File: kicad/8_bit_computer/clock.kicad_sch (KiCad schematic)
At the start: 0 parts

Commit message: Astable clock
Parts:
- added C4: 220uF, Capacitor_THT:CP_Radial_D10.0mm_P5.00mm, symbol Device:C_Polarized_US
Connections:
- new net +5V: C4.1
- new net GND: C4.2
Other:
- added sheet Astable Timer (astable_timer.kicad_sch)
- title: (none) -> Clock Module

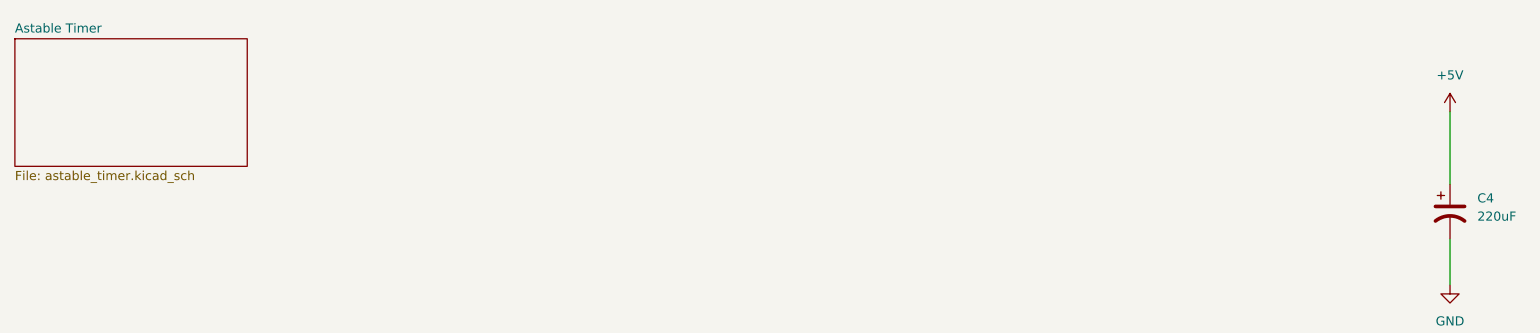
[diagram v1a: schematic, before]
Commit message: Bistable and Monstable Clocks
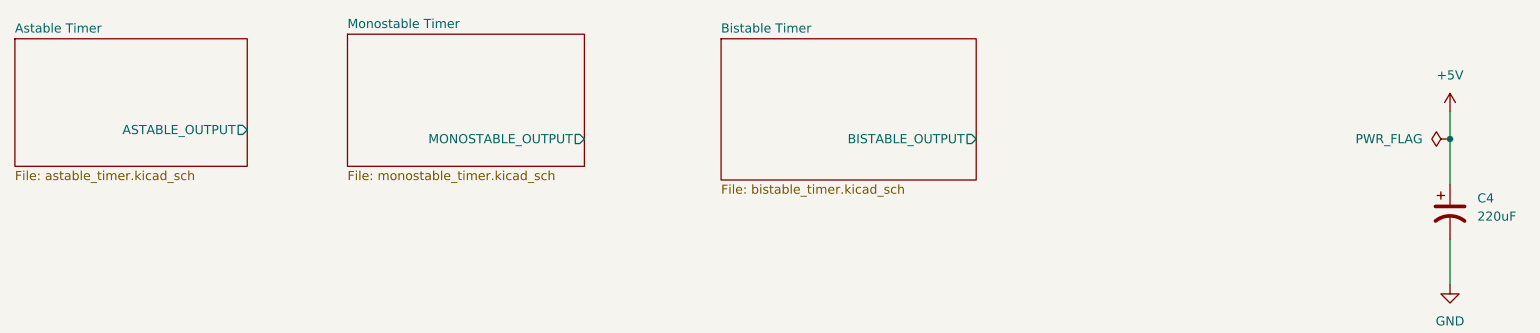
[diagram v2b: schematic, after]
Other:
- added sheet Bistable Timer (bistable_timer.kicad_sch)
- added sheet Monostable Timer (monostable_timer.kicad_sch)
- sheet Astable Timer ports: added ASTABLE_OUTPUT; removed none
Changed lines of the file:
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@@
 		(rev "0")
+	)
+	(junction
+		(at 245.11 44.45)
+		(diameter 0)
+		(color 0 0 0 0)
 	)
 	(wire
 		(pts
-			(xy 245.11 40.64) (xy 245.11 50.8)
+			(xy 245.11 40.64) (xy 245.11 44.45)
 		)
 		(stroke
@@
 		(pts
 			(xy 245.11 58.42) (xy 245.11 64.77)
+		)
+		(stroke
+			(width 0)
+			(type default)
+		)
+	)
+	(wire
+		(pts
+			(xy 245.11 44.45) (xy 245.11 50.8)
 		)
 		(stroke
@@
 	)
 	(symbol
+		(lib_id "power:PWR_FLAG")
+		(at 245.11 44.45 90)
+		(unit 1)
+		(exclude_from_sim no)
+		(in_bom yes)
+		(on_board yes)
+		(dnp no)
+		(fields_autoplaced yes)
+		(property "Reference" "#FLG03"
+			(at 243.205 44.45 0)
+			(effects
+				(font
+					(size 1.27 1.27)
+				)
+				(hide yes)
+			)
+		)
+		(property "Value" "PWR_FLAG"
+			(at 241.3 44.4499 90)
+			(effects
+				(font
+					(size 1.27 1.27)
+				)
+				(justify left)
+			)
+		)
+		(property "Footprint" ""
+			(at 245.11 44.45 0)
+			(effects
+				(font
+					(size 1.27 1.27)
+				)
+				(hide yes)
+			)
+		)
+		(property "Datasheet" "~"
+			(at 245.11 44.45 0)
+			(effects
+				(font
+					(size 1.27 1.27)
+				)
+				(hide yes)
+			)
+		)
+		(property "Description" "Special symbol for telling ERC where power comes from"
+			(at 245.11 44.45 0)
+			(effects
+				(font
+					(size 1.27 1.27)
+				)
+				(hide yes)
+			)
+		)
+		(pin "1"
+		)
+		(instances
+			(project ""
+				(path "/24dbb59b-fc31-4588-b2ee-d18f20639e07/62eb35ce-6b42-428c-8bc5-4f1b242b0bef"
+					(reference "#FLG03")
+					(unit 1)
+				)
+			)
+		)
+	)
+	(symbol
 		(lib_id "Device:C_Polarized_US")
 		(at 245.11 54.61 0)
@@
 			)
 		)
+		(pin "ASTABLE_OUTPUT" output
+			(at 77.47 43.18 0)
+			(effects
+				(font
+					(size 1.27 1.27)
+				)
+				(justify right)
+			)
+		)
 		(instances
 			(project "8_bit_computer"
@@
 				)
 			)
+		)
+	)
+	(sheet
+		(at 143.51 30.48)
+		(size 35.56 19.685)
+		(fields_autoplaced yes)
+		(stroke
+			(width 0.1524)
+			(type solid)
+		)
+		(fill
+			(color 0 0 0 0.0000)
+		)
+		(property "Sheetname" "Bistable Timer"
+			(at 143.51 29.7684 0)
+			(effects
+				(font
+					(size 1.27 1.27)
+				)
+				(justify left bottom)
+			)
+		)
+		(property "Sheetfile" "bistable_timer.kicad_sch"
+			(at 143.51 50.7496 0)
+			(effects
+				(font
+					(size 1.27 1.27)
+				)
+				(justify left top)
+			)
+		)
+		(pin "BISTABLE_OUTPUT" output
+			(at 179.07 44.45 0)
+			(effects
+				(font
+					(size 1.27 1.27)
+				)
+				(justify right)
+			)
+		)
+		(instances
+			(project "8_bit_computer"
+				(path "/24dbb59b-fc31-4588-b2ee-d18f20639e07/62eb35ce-6b42-428c-8bc5-4f1b242b0bef"
+					(page "5")
+				)
+			)
+		)
+	)
+	(sheet
+		(at 91.44 29.845)
+		(size 33.02 18.415)
+		(fields_autoplaced yes)
+		(stroke
+			(width 0.1524)
+			(type solid)
+		)
+		(fill
+			(color 0 0 0 0.0000)
+		)
+		(property "Sheetname" "Monostable Timer"
+			(at 91.44 29.1334 0)
+			(effects
+				(font
+					(size 1.27 1.27)
+				)
+				(justify left bottom)
+			)
+		)
+		(property "Sheetfile" "monostable_timer.kicad_sch"
+			(at 91.44 48.8446 0)
+			(effects
+				(font
+					(size 1.27 1.27)
+				)
+				(justify left top)
+			)
+		)
+		(pin "MONOSTABLE_OUTPUT" output
+			(at 124.46 44.45 0)
+			(effects
+				(font
+					(size 1.27 1.27)
+				)
+				(justify right)
+			)
+		)
+		(instances
+			(project "8_bit_computer"
+				(path "/24dbb59b-fc31-4588-b2ee-d18f20639e07/62eb35ce-6b42-428c-8bc5-4f1b242b0bef"
+					(page "4")
+				)
+			)

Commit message: Functional 8 bit computer clock
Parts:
- added C10, C12, C13: 0.1 uF, Capacitor_THT:C_Disc_D5.0mm_W2.5mm_P2.50mm, symbol Device:C
- added D4: LED Blue, LED_THT:LED_D5.0mm, symbol Device:LED
- added R5: 220, Resistor_THT:R_Axial_DIN0207_L6.3mm_D2.5mm_P7.62mm_Horizontal, symbol Device:R
- added U4: 74LS32, Package_DIP:DIP-14_W7.62mm, symbol 74xx:74LS32
- added U5: 74LS08, Package_DIP:DIP-14_W7.62mm, symbol 74xx:74LS08
- added U6: 74LS04, Package_DIP:DIP-14_W7.62mm, symbol 74xx:74LS04
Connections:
- net +5V: now also C10.2, C12.2, C13.2, U4.14 (VCC), U5.14 (VCC), U6.14 (VCC)
- net Astable Timer/ASTABLE_OUTPUT: now also U5.1
- net Bistable Timer/BISTABLE_OUTPUT: now also U5.2, U6.1
- net GND: now also C10.1, C12.1, C13.1, R5.2, U4.10, U4.12, U4.13, U4.4, U4.5, U4.7 (GND), U4.9, U5.12, U5.13, U5.7 (GND), U6.11, U6.5, U6.7 (GND), U6.9
- net Monostable Timer/MONOSTABLE_OUTPUT: now also U5.5
- new net: U5.4, U6.2
- new net: U4.2, U5.6
- new net: U5.10, U6.4
- new net: U4.1, U5.3
- new net: D4.1 (K), R5.1
- new net: U4.3, U5.9
- new net CLK: D4.2 (A), U5.8, U6.13
- new net HLT: U6.3
- new net ~{CLK}: U6.12
- no-connect marks 0 -> 7
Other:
- note added: "Unused"
- moved on the sheet: C4

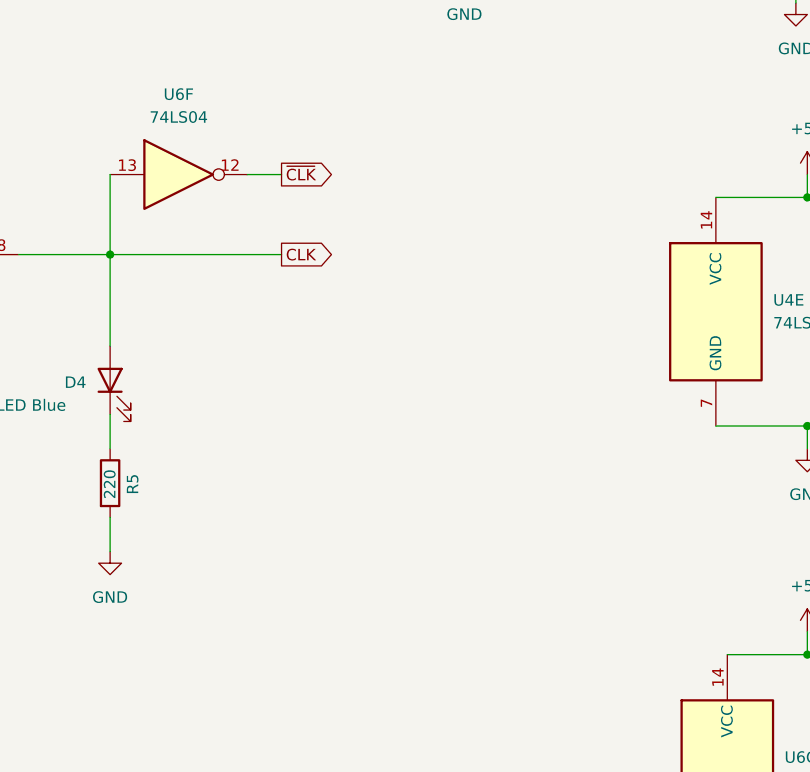
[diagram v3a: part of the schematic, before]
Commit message: clk_n indicator led
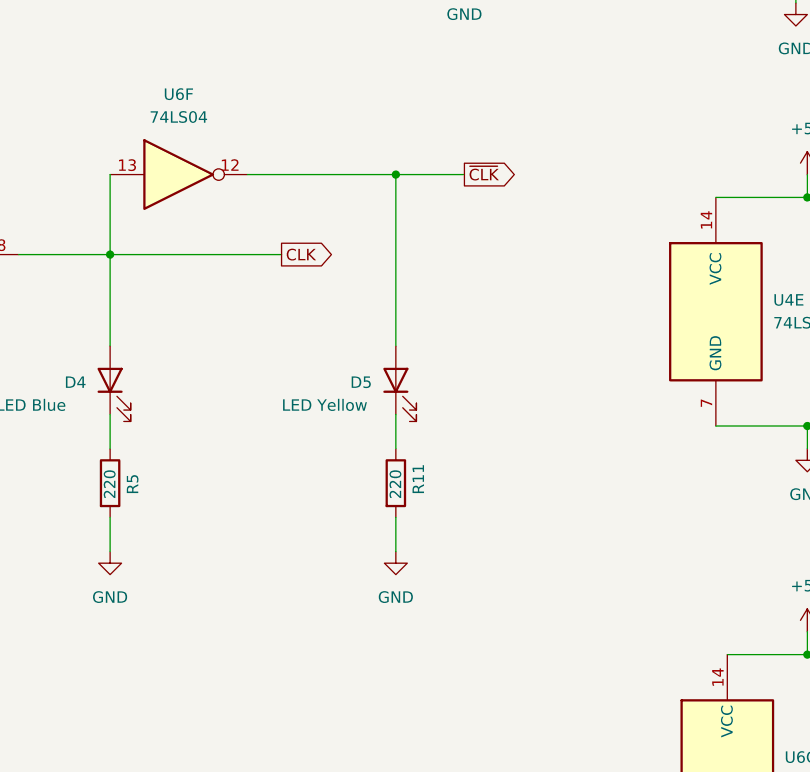
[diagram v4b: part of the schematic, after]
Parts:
- added D5: LED Yellow, LED_THT:LED_D5.0mm, symbol Device:LED
- added R11: 220, Resistor_THT:R_Axial_DIN0207_L6.3mm_D2.5mm_P7.62mm_Horizontal, symbol Device:R
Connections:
- net GND: now also R11.2
- net ~{CLK}: now also D5.2 (A)
- new net: D5.1 (K), R11.1

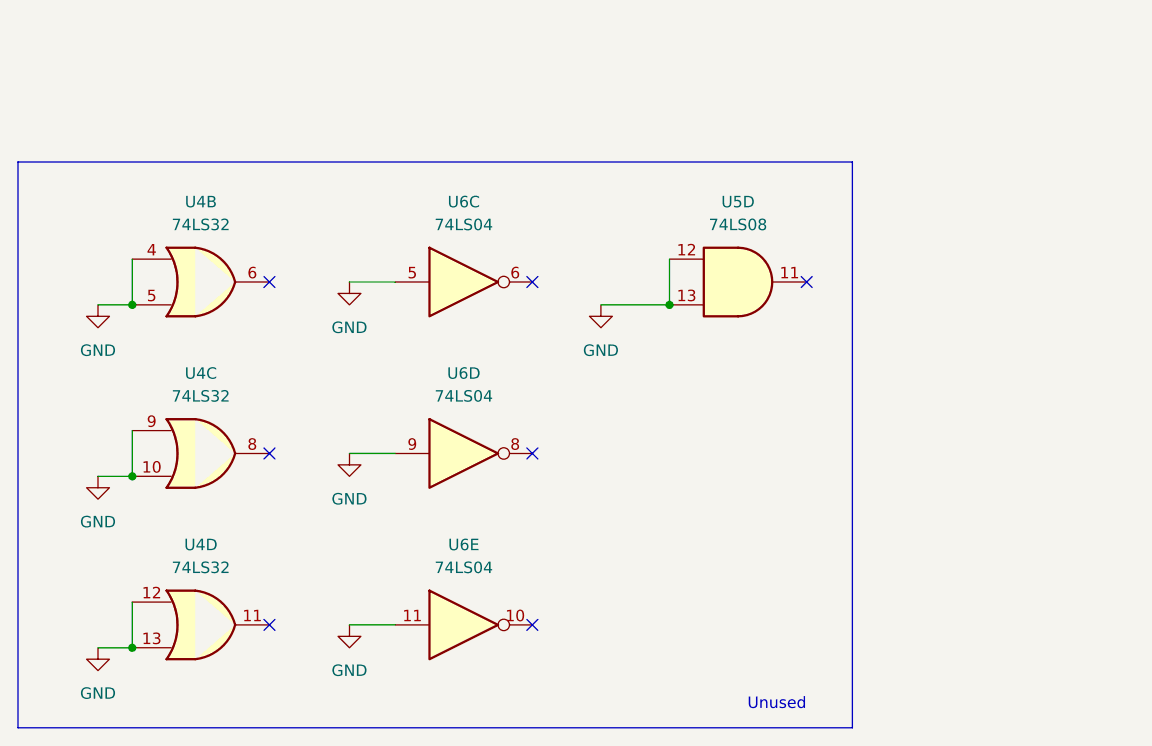
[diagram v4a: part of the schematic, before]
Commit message: Use pull down resistors instead of shorting to gnd
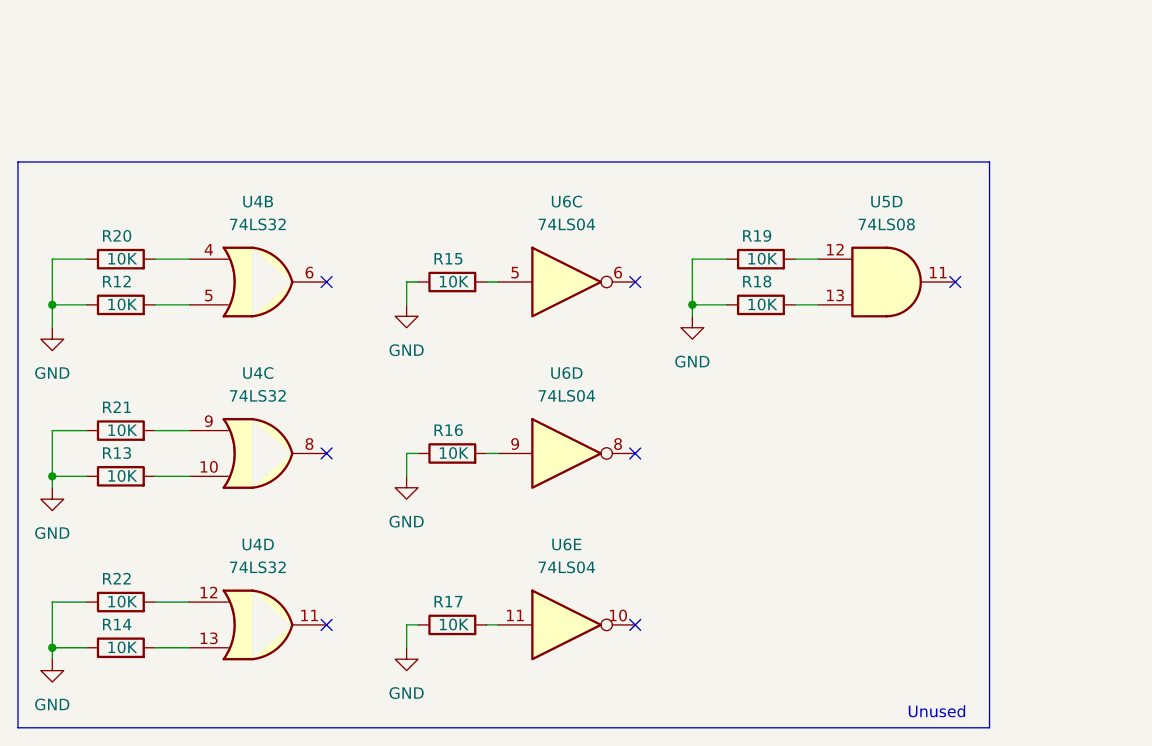
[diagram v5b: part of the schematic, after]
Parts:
- added R12, R13, R14, R15, R16, R17, R18, R19, R20, R21, R22: 10K, Resistor_THT:R_Axial_DIN0207_L6.3mm_D2.5mm_P7.62mm_Horizontal, symbol Device:R
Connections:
- net GND: now also R12.1, R13.1, R14.1, R15.1, R16.1, R17.1, R18.1, R19.1, R20.1, R21.1, R22.1; no longer U4.10, U4.12, U4.13, U4.4, U4.5, U4.9, U5.12, U5.13, U6.11, U6.5, U6.9
- new net: R16.2, U6.9
- new net: R17.2, U6.11
- new net: R15.2, U6.5
- new net: R22.2, U4.12
- new net: R13.2, U4.10
- new net: R21.2, U4.9
- new net: R14.2, U4.13
- new net: R20.2, U4.4
- new net: R12.2, U4.5
- new net: R18.2, U5.13
- new net: R19.2, U5.12
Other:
- moved on the sheet: U4B, U4C, U4D, U5D, U6C, U6D, U6E

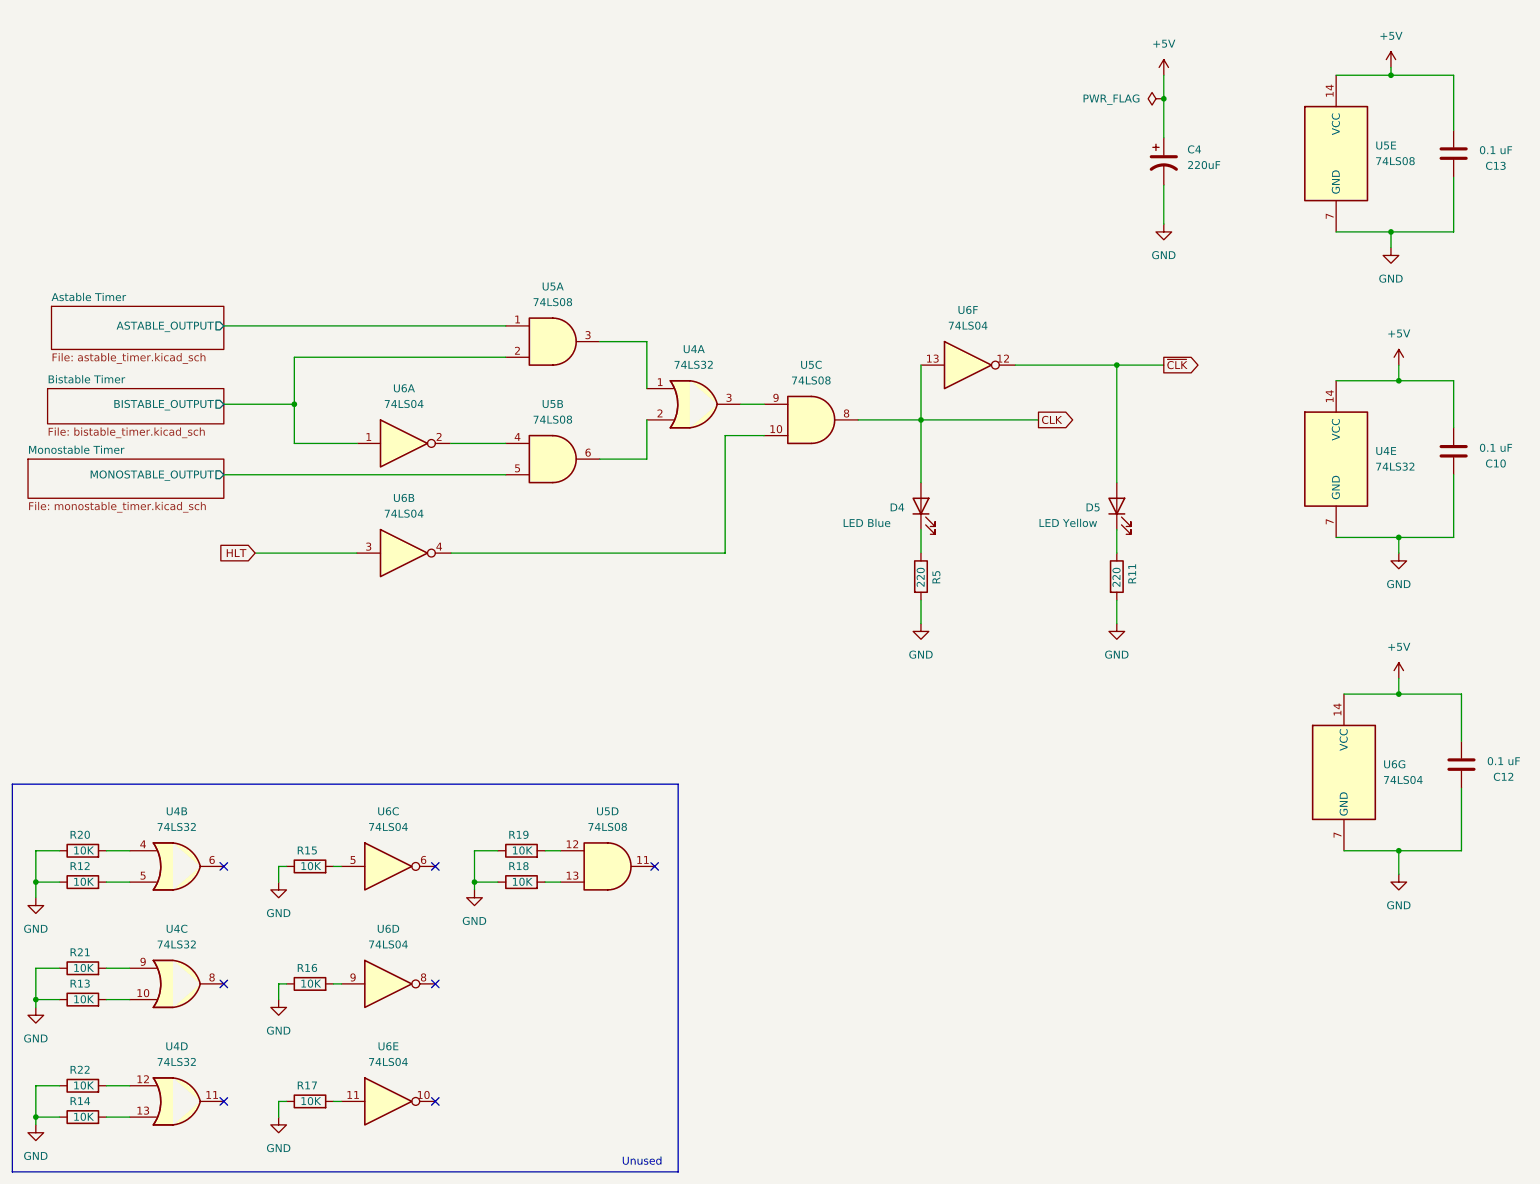
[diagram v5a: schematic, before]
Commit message: Mostly implemented register, still ERC errors
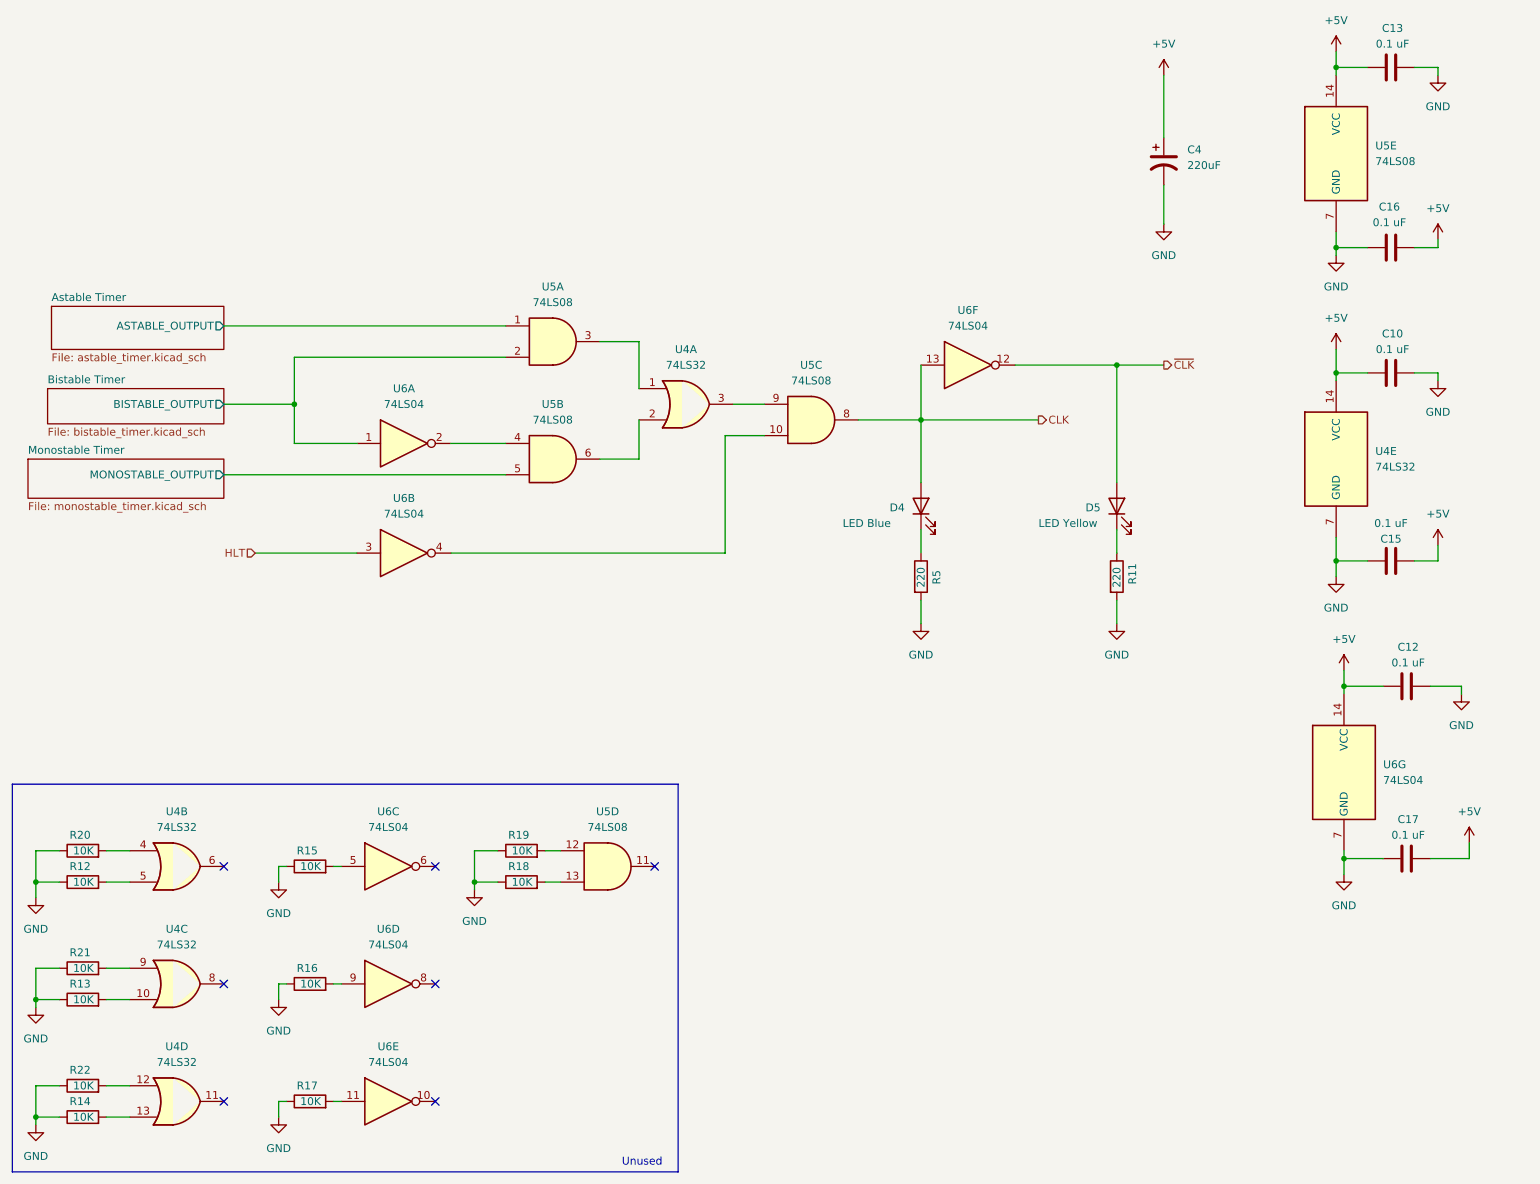
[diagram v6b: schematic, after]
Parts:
- added C15, C16, C17: 0.1 uF, Capacitor_THT:C_Disc_D5.0mm_W2.5mm_P2.50mm, symbol Device:C
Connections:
- net +5V: now also C15.1, C16.1, C17.1
- net GND: now also C15.2, C16.2, C17.2
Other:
- moved on the sheet: C10, C12, C13, U4A

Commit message: Fix all erc errors
I had to delete and re-add a component that must have been placed on a
different grid. No amount of aligning to the grid would fix it.
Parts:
- removed U5: 74LS08, Package_DIP:DIP-14_W7.62mm, symbol 74xx:74LS08
- added U10: 74LS08, Package_DIP:DIP-14_W7.62mm, symbol 74xx:74LS08
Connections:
- net +5V: now also U10.14 (VCC)
- net Astable Timer/ASTABLE_OUTPUT: now also U10.1
- net Bistable Timer/BISTABLE_OUTPUT: now also U10.2
- net CLK: now also U10.8
- net GND: now also U10.7 (GND)
- net Monostable Timer/MONOSTABLE_OUTPUT: now also U10.5
- net at U6.2: now also U10.4
- net at U4.2: now also U10.6
- net at R18.2: now also U10.13
- net at R19.2: now also U10.12
- net at U6.4: now also U10.10
- net at U4.1: now also U10.3
- net at U4.3: now also U10.9
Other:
- moved on the sheet: U6A
